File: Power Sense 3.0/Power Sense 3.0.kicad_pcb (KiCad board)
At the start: 2 copper layers, 133.9 x 50.3 mm, 49 parts, among them IC1 MCP3909, J1 Power, J2 ProgHead, J3 SPI, J4 TestHeader, T1 AC1030, T2 2p2sTransformer, U1 PIC18F25K20_I/SS, Y1 3.579545MHz Crystal

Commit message: 3.1.1
Edited Test Header Connection
Changed resistor value
See README.txt for more info
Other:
- board text added: "Power Sense 3.1.1"
- board text removed: "Power Sense 3.1"
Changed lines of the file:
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@@
   )
   (gr_line (start 107.569 54.229) (end 107.569 52.705) (layer F.SilkS) (width 0.2))
-  (gr_text "Power Sense 3.1" (at 159.131 56.3245) (layer F.SilkS)
+  (gr_text "Power Sense 3.1.1" (at 159.131 56.3245) (layer F.SilkS)
     (effects (font (size 1.75 1.75) (thickness 0.35)))
   )

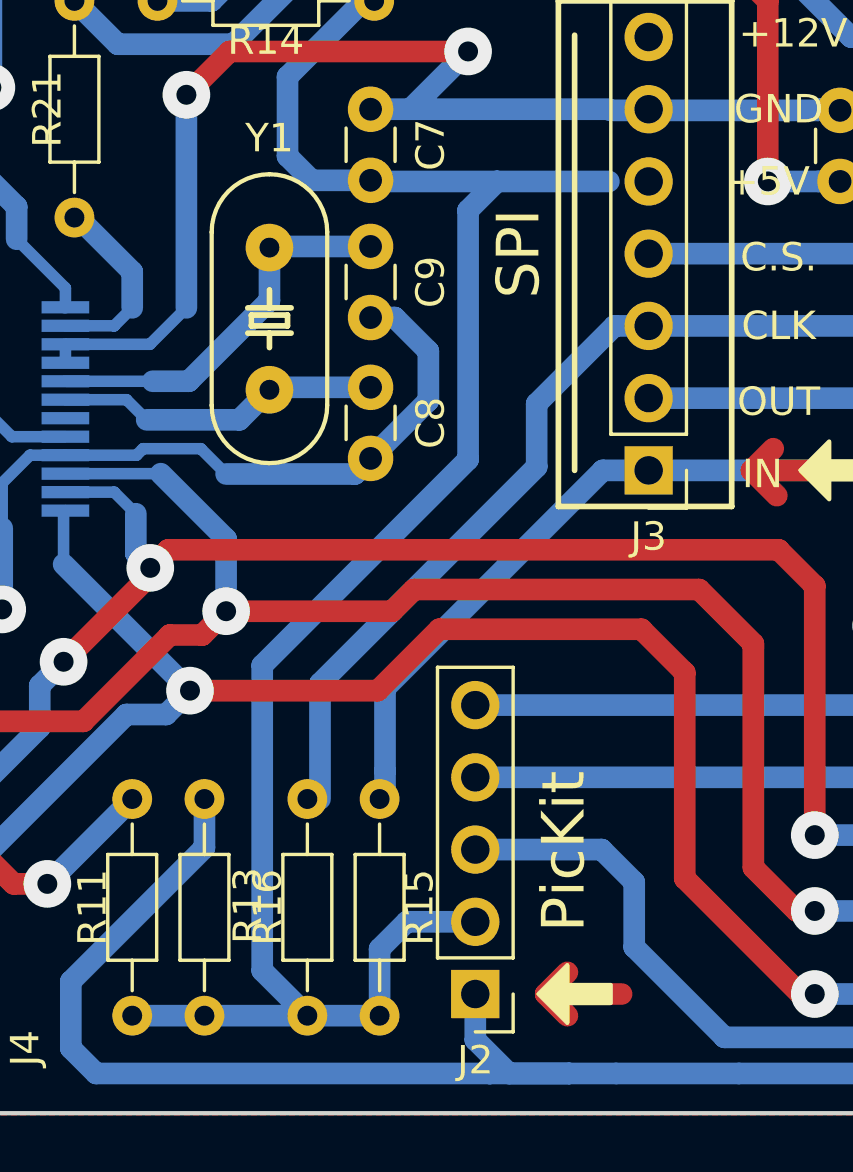
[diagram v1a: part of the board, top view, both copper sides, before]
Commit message: 3.1.2
Removed two resistors in SCH and PCB
Fixed 5V connection on SPI connector
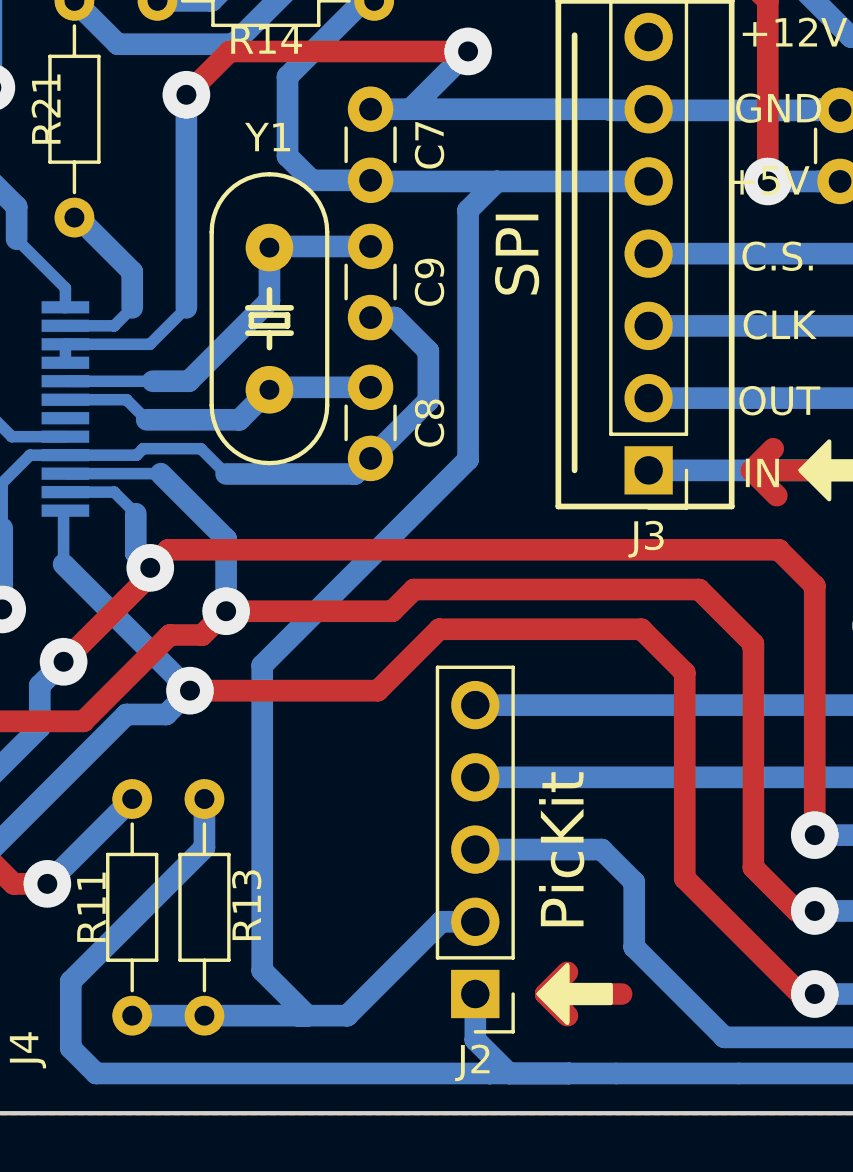
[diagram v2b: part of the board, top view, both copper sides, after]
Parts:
- removed R15, R16: 10, Resistors_THT:R_Axial_DIN0204_L3.6mm_D1.6mm_P7.62mm_Horizontal
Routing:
- net /SPI_CLK: track 33.2 -> 11.0 mm
- net /SPI_MD_IN: track 27.4 -> 11.0 mm

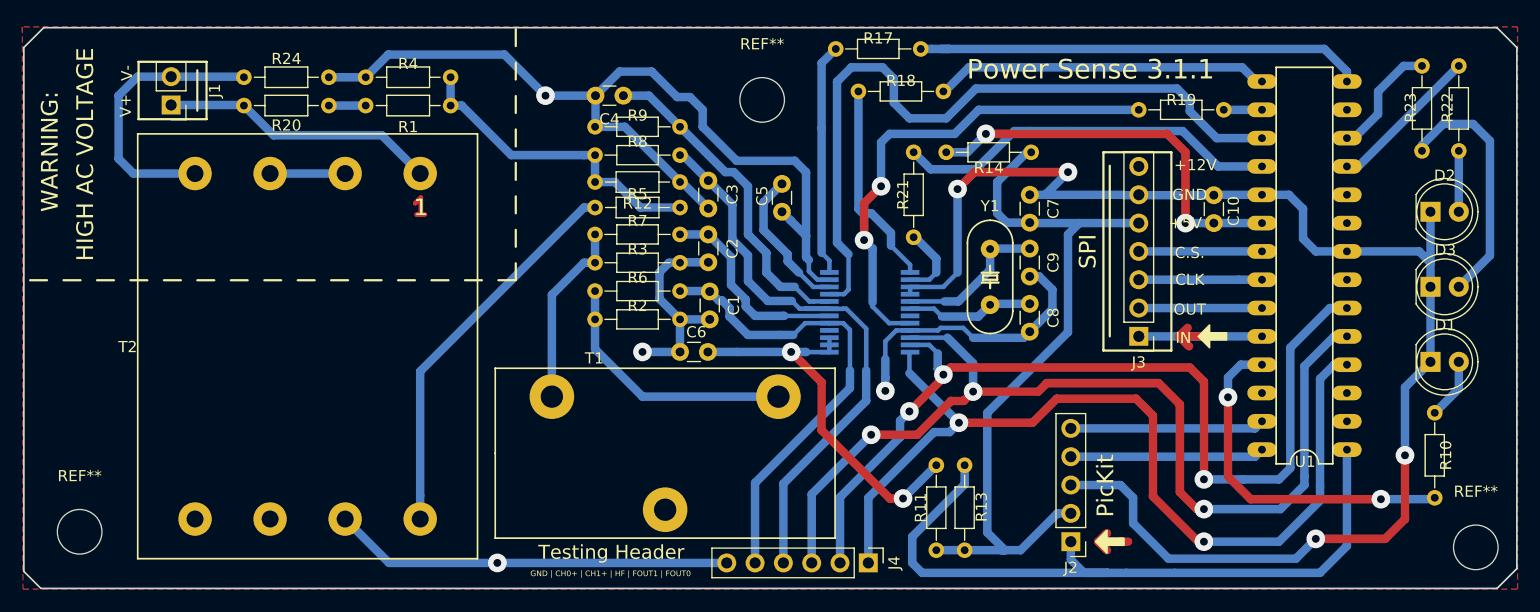
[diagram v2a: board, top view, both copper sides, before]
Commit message: 3.1.2
Updated Silkscreen Labels
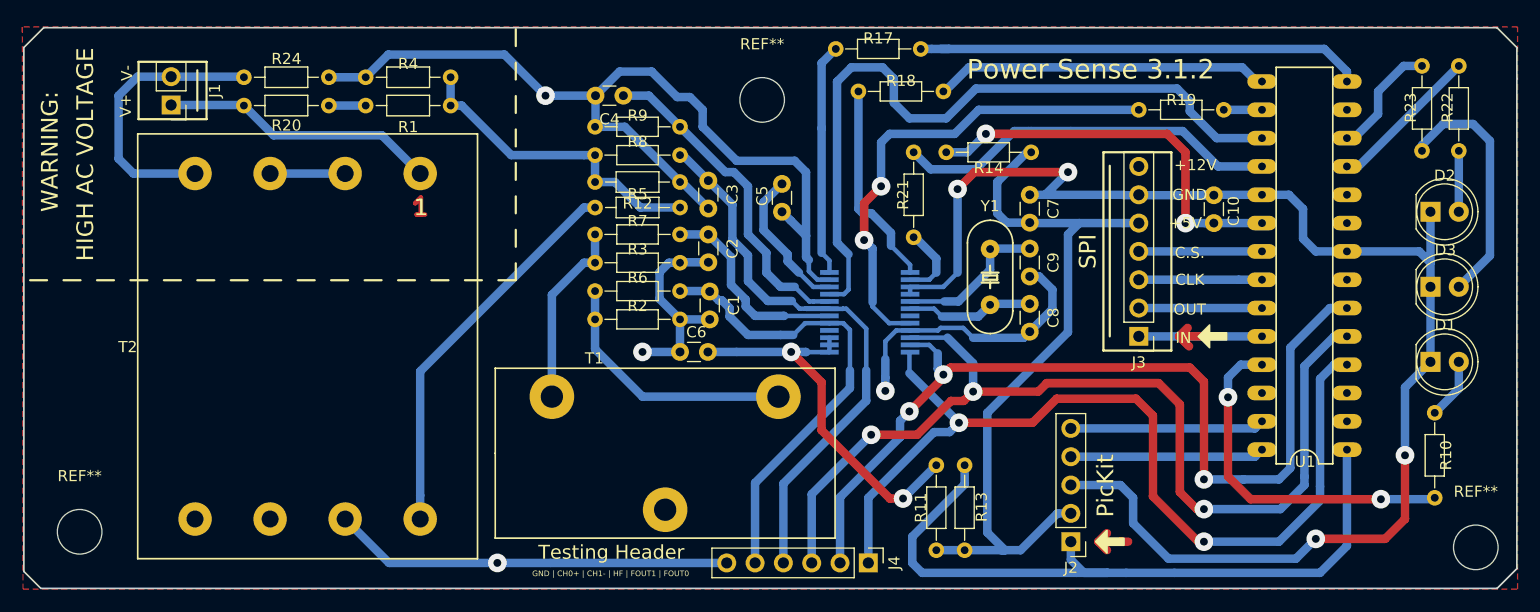
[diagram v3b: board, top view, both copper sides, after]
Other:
- board text added: "GND | CH0+ | CH1- | HF | FOUT1 | FOUT0"
- board text added: "Power Sense 3.1.2"
- board text removed: "GND | CH0+ | CH1+ | HF | FOUT1 | FOUT0"
- board text removed: "Power Sense 3.1.1"
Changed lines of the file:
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@@
     (effects (font (size 1.25 1.25) (thickness 0.2)))
   )
-  (gr_text "GND | CH0+ | CH1+ | HF | FOUT1 | FOUT0" (at 116.078 101.5365) (layer F.SilkS)
+  (gr_text "GND | CH0+ | CH1- | HF | FOUT1 | FOUT0" (at 116.078 101.5365) (layer F.SilkS)
     (effects (font (size 0.5 0.5) (thickness 0.125)))
   )
@@
   )
   (gr_line (start 107.569 54.229) (end 107.569 52.705) (layer F.SilkS) (width 0.2))
-  (gr_text "Power Sense 3.1.1" (at 159.131 56.3245) (layer F.SilkS)
+  (gr_text "Power Sense 3.1.2" (at 159.131 56.3245) (layer F.SilkS)
     (effects (font (size 1.75 1.75) (thickness 0.35)))
   )

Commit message: Silkscreen fix
Add silkscreen to the power sense board.
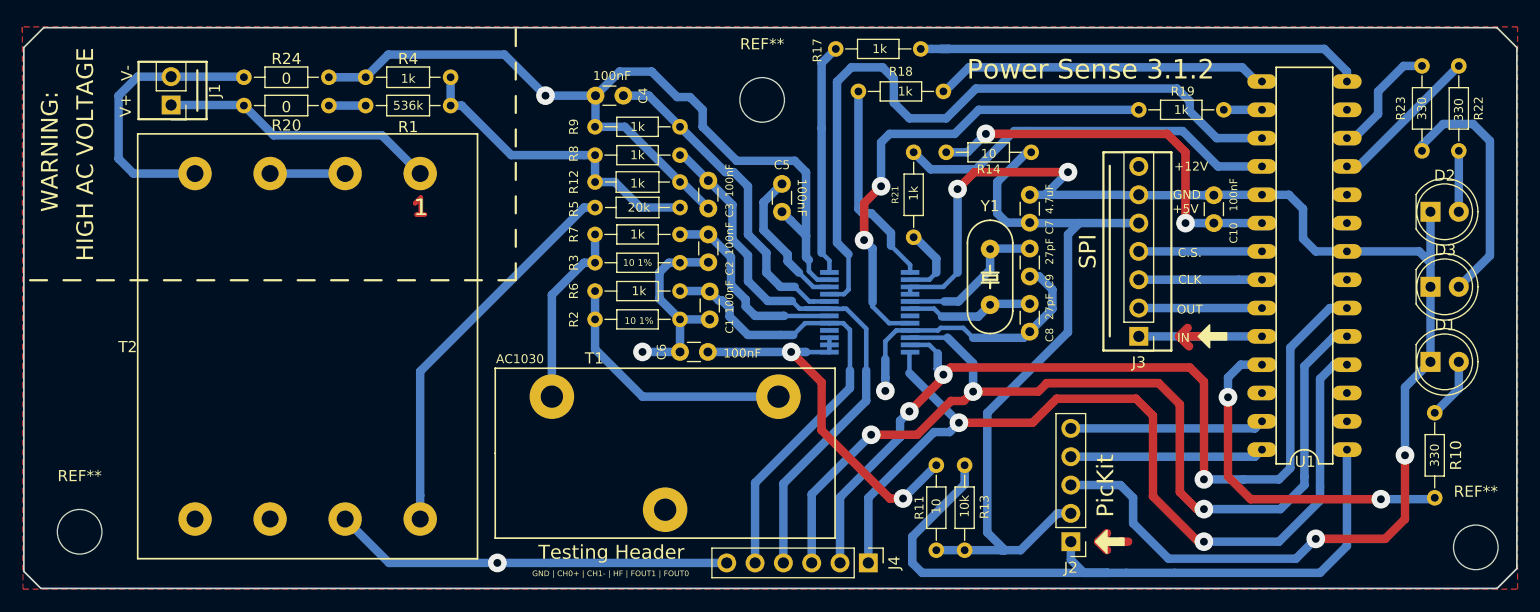
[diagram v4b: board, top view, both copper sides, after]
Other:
- board text added: "0"
- board text added: "10"
- board text added: "10 1%"
- board text added: "100nF"
- board text added: "10k"
- board text added: "1k"
- board text added: "20k"
- board text added: "27pF"
- board text added: "330"
- board text added: "4.7uF"
- board text added: "536k"
- board text added: "AC1030"

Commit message: PCB Fix
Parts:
- moved T2 0.51 mm to (88.4, 81.2)
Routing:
- net GND: track 300.6 -> 307.0 mm
- net Net-(C5-Pad1): track 13.2 -> 14.2 mm
- net /CH1-: track 52.6 -> 53.3 mm
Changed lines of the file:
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@@
     (thickness 1.6)
     (drawings 103)
-    (tracks 464)
+    (tracks 471)
     (zones 0)
     (modules 47)
@@
   )
   (module "EMMS_FP:Transformer FS12-090-C2" (layer F.Cu)
-    (at 88.9 81.153 180)
+    (at 88.392 81.153 180)
     (fp_text reference T2 (at 16.129 -0.0635 180) (layer F.SilkS)
       (effects (font (size 1 1) (thickness 0.15)))
@@
   (via (at 110.236 58.674) (size 1.6764) (drill 0.7) (layers F.Cu B.Cu) (net 1))
   (segment (start 153.67 74.89) (end 154.519 74.89) (width 0.762) (layer B.Cu) (net 1) (status 10))
-  (segment (start 155.702 77.811) (end 153.67 79.843) (width 0.762) (layer B.Cu) (net 1) (status 20))
-  (segment (start 155.702 76.073) (end 155.702 77.811) (width 0.762) (layer B.Cu) (net 1))
   (segment (start 154.519 74.89) (end 155.702 76.073) (width 0.762) (layer B.Cu) (net 1))
   (segment (start 187.325 90.932) (end 187.325 84.836) (width 0.762) (layer B.Cu) (net 1))
@@
   (segment (start 131.445 69.088) (end 132.244999 69.887999) (width 0.762) (layer B.Cu) (net 1) (status 10))
   (segment (start 133.604 73.152) (end 133.604 71.247) (width 0.762) (layer B.Cu) (net 1))
-  (segment (start 116.88 56.515) (end 114.721 58.674) (width 0.762) (layer B.Cu) (net 1) (status 20))
-  (segment (start 119.761 56.515) (end 116.88 56.515) (width 0.762) (layer B.Cu) (net 1))
-  (segment (start 122.047 58.801) (end 119.761 56.515) (width 0.762) (layer B.Cu) (net 1))
-  (segment (start 133.604 65.532) (end 132.588 64.516) (width 0.762) (layer B.Cu) (net 1))
-  (segment (start 133.604 71.247) (end 133.604 65.532) (width 0.762) (layer B.Cu) (net 1))
-  (segment (start 123.19 58.801) (end 122.047 58.801) (width 0.762) (layer B.Cu) (net 1))
-  (segment (start 132.588 64.516) (end 127.381 64.516) (width 0.762) (layer B.Cu) (net 1))
-  (segment (start 127.381 64.516) (end 124.333 61.468) (width 0.762) (layer B.Cu) (net 1))
-  (segment (start 124.333 61.468) (end 124.333 59.944) (width 0.762) (layer B.Cu) (net 1))
-  (segment (start 124.333 59.944) (end 123.19 58.801) (width 0.762) (layer B.Cu) (net 1))
   (segment (start 90.805 57.023) (end 94.107 57.023) (width 0.762) (layer B.Cu) (net 1))
   (segment (start 106.553 54.991) (end 110.236 58.674) (width 0.762) (layer B.Cu) (net 1))
@@
   (segment (start 140.716 83.968107) (end 140.716 82.296) (width 0.762) (layer B.Cu) (net 1))
   (segment (start 140.716 85.1535) (end 140.716 83.968107) (width 0.762) (layer B.Cu) (net 1))
-  (segment (start 121.311051 73.66) (end 120.4595 74.511551) (width 0.762) (layer B.Cu) (net 1))
-  (segment (start 122.301 73.66) (end 121.311051 73.66) (width 0.762) (layer B.Cu) (net 1))
-  (segment (start 120.4595 74.511551) (end 120.4595 76.8985) (width 0.762) (layer B.Cu) (net 1))
-  (segment (start 120.4595 76.8985) (end 122.301 78.74) (width 0.762) (layer B.Cu) (net 1))
-  (segment (start 117.348 61.468) (end 122.301 66.421) (width 0.762) (layer B.Cu) (net 1))
-  (segment (start 114.681 61.468) (end 117.348 61.468) (width 0.762) (layer B.Cu) (net 1))
   (segment (start 96.2025 100.584) (end 110.6805 100.584) (width 0.762) (layer B.Cu) (net 1))
   (segment (start 92.2655 96.647) (end 96.2025 100.584) (width 0.762) (layer B.Cu) (net 1))
   (segment (start 118.9355 81.661) (end 122.301 81.661) (width 0.762) (layer B.Cu) (net 1))
   (segment (start 110.6805 100.584) (end 126.492 100.584) (width 0.762) (layer B.Cu) (net 1))
+  (segment (start 121.2215 78.74) (end 122.301 78.74) (width 0.762) (layer B.Cu) (net 1))
+  (segment (start 119.38 76.8985) (end 121.2215 78.74) (width 0.762) (layer B.Cu) (net 1))
+  (segment (start 119.38 74.511551) (end 119.38 76.8985) (width 0.762) (layer B.Cu) (net 1))
+  (segment (start 122.301 73.66) (end 120.231551 73.66) (width 0.762) (layer B.Cu) (net 1))
+  (segment (start 120.231551 73.66) (end 119.38 74.511551) (width 0.762) (layer B.Cu) (net 1))
+  (segment (start 133.604 65.532) (end 133.604 71.247) (width 0.762) (layer B.Cu) (net 1))
+  (segment (start 132.588 64.516) (end 133.604 65.532) (width 0.762) (layer B.Cu) (net 1))
+  (segment (start 127.381 64.516) (end 132.588 64.516) (width 0.762) (layer B.Cu) (net 1))
+  (segment (start 114.721 58.674) (end 114.721 55.459) (width 0.762) (layer B.Cu) (net 1))
+  (segment (start 114.721 55.459) (end 115.57 54.61) (width 0.762) (layer B.Cu) (net 1))
+  (segment (start 115.57 54.61) (end 118.999 54.61) (width 0.762) (layer B.Cu) (net 1))
+  (segment (start 118.999 54.61) (end 124.333 59.944) (width 0.762) (layer B.Cu) (net 1))
+  (segment (start 124.333 59.944) (end 124.333 61.468) (width 0.762) (layer B.Cu) (net 1))
+  (segment (start 124.333 61.468) (end 127.381 64.516) (width 0.762) (layer B.Cu) (net 1))
+  (segment (start 122.301 66.421) (end 121.031 66.421) (width 0.762) (layer B.Cu) (net 1))
+  (segment (start 121.031 66.421) (end 116.84 62.23) (width 0.762) (layer B.Cu) (net 1))
+  (segment (start 114.681 61.468) (end 116.078 61.468) (width 0.762) (layer B.Cu) (net 1))
+  (segment (start 116.078 61.468) (end 116.84 62.23) (width 0.762) (layer B.Cu) (net 1))
+  (segment (start 153.67 79.843) (end 154.80137 79.843) (width 0.762) (layer B.Cu) (net 1))
+  (segment (start 155.702 76.073) (end 155.702 79.248) (width 0.762) (layer B.Cu) (net 1))
+  (segment (start 155.107 79.843) (end 154.80137 79.843) (width 0.762) (layer B.Cu) (net 1))
+  (segment (start 155.702 79.248) (end 155.107 79.843) (width 0.762) (layer B.Cu) (net 1))
   (segment (start 135.6995 78.430001) (end 131.627999 78.430001) (width 0.4064) (layer B.Cu) (net 2) (status 10))
   (segment (start 122.301 71.12) (end 124.841 71.12) (width 0.762) (layer B.Cu) (net 2) (status 30))
@@
   (segment (start 134.250001 75.830001) (end 132.969 74.549) (width 0.4064) (layer B.Cu) (net 3))
   (segment (start 134.250001 75.830001) (end 135.6995 75.830001) (width 0.4064) (layer B.Cu) (net 3) (status 20))
-  (segment (start 129.794 68.239) (end 131.445 66.588) (width 0.762) (layer B.Cu) (net 3) (status 20))
-  (segment (start 129.794 68.239) (end 129.794 70.739) (width 0.762) (layer B.Cu) (net 3))
-  (segment (start 129.794 70.739) (end 131.953 72.898) (width 0.762) (layer B.Cu) (net 3))
   (segment (start 131.953 73.533) (end 132.969 74.549) (width 0.762) (layer B.Cu) (net 3))
   (segment (start 131.953 72.898) (end 131.953 73.533) (width 0.762) (layer B.Cu) (net 3))
+  (segment (start 129.54 70.485) (end 131.953 72.898) (width 0.762) (layer B.Cu) (net 3))
+  (segment (start 129.54 67.136) (end 129.54 70.485) (width 0.762) (layer B.Cu) (net 3))
+  (segment (start 131.445 66.588) (end 130.088 66.588) (width 0.762) (layer B.Cu) (net 3))
+  (segment (start 130.088 66.588) (end 129.54 67.136) (width 0.762) (layer B.Cu) (net 3))
   (via (at 142.3035 94.8055) (size 1.6764) (drill 0.7) (layers F.Cu B.Cu) (net 4))
   (segment (start 135.6995 81.03) (end 135.6995 80.380002) (width 0.4064) (layer B.Cu) (net 4) (status 30))
@@
   (segment (start 122.555 64.008) (end 124.841 66.294) (width 0.762) (layer B.Cu) (net 56) (status 30))
   (segment (start 122.301 64.008) (end 122.555 64.008) (width 0.762) (layer B.Cu) (net 56) (status 30))
-  (segment (start 127 68.453) (end 124.841 66.294) (width 0.762) (layer B.Cu) (net 56))
-  (segment (start 127 71.596013) (end 127 68.453) (width 0.762) (layer B.Cu) (net 56))
-  (segment (start 128.397 72.993013) (end 127 71.596013) (width 0.762) (layer B.Cu) (net 56))
-  (segment (start 128.397 75.311) (end 128.397 72.993013) (width 0.762) (layer B.Cu) (net 56))
-  (segment (start 132.334 77.089) (end 130.175 77.089) (width 0.762) (layer B.Cu) (net 56))
-  (segment (start 130.175 77.089) (end 128.397 75.311) (width 0.762) (layer B.Cu) (net 56))
   (segment (start 139.0015 83.312) (end 139.0015 86.0425) (width 0.762) (layer B.Cu) (net 56))
   (segment (start 131.572 93.472) (end 131.572 100.584) (width 0.762) (layer B.Cu) (net 56))
@@
   (segment (start 133.620699 77.780002) (end 133.639799 77.799102) (width 0.4064) (layer B.Cu) (net 56))
   (segment (start 133.533002 77.780002) (end 133.620699 77.780002) (width 0.4064) (layer B.Cu) (net 56))
+  (segment (start 128.397 75.311) (end 130.175 77.089) (width 0.762) (layer B.Cu) (net 56))
+  (segment (start 130.175 77.089) (end 132.334 77.089) (width 0.762) (layer B.Cu) (net 56))
+  (segment (start 125.73 67.183) (end 126.873 67.183) (width 0.762) (layer B.Cu) (net 56))
+  (segment (start 124.841 66.294) (end 125.73 67.183) (width 0.762) (layer B.Cu) (net 56))
+  (segment (start 126.873 67.183) (end 127 67.31) (width 0.762) (layer B.Cu) (net 56))
+  (segment (start 127 67.31) (end 127 71.596013) (width 0.762) (layer B.Cu) (net 56))
+  (segment (start 127 71.596013) (end 128.397 72.993013) (width 0.762) (layer B.Cu) (net 56))
+  (segment (start 128.397 72.993013) (end 128.397 75.311) (width 0.762) (layer B.Cu) (net 56))
   (zone (net 1) (net_name GND) (layer F.Cu) (hatch edge 0.508)
     (connect_pads (clearance 0.508))
